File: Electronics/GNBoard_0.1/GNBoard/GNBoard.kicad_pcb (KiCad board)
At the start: 2 copper layers, 77.9 x 54.5 mm, 47 parts, among them K1 IR1, K10 IR4, K11 CNY_1, K12 CNY_2, K13 CNY_3, K14 CNY_4, K15 CNY_5, K16 CNY_6, K2 IR2, K3 SERVO_1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

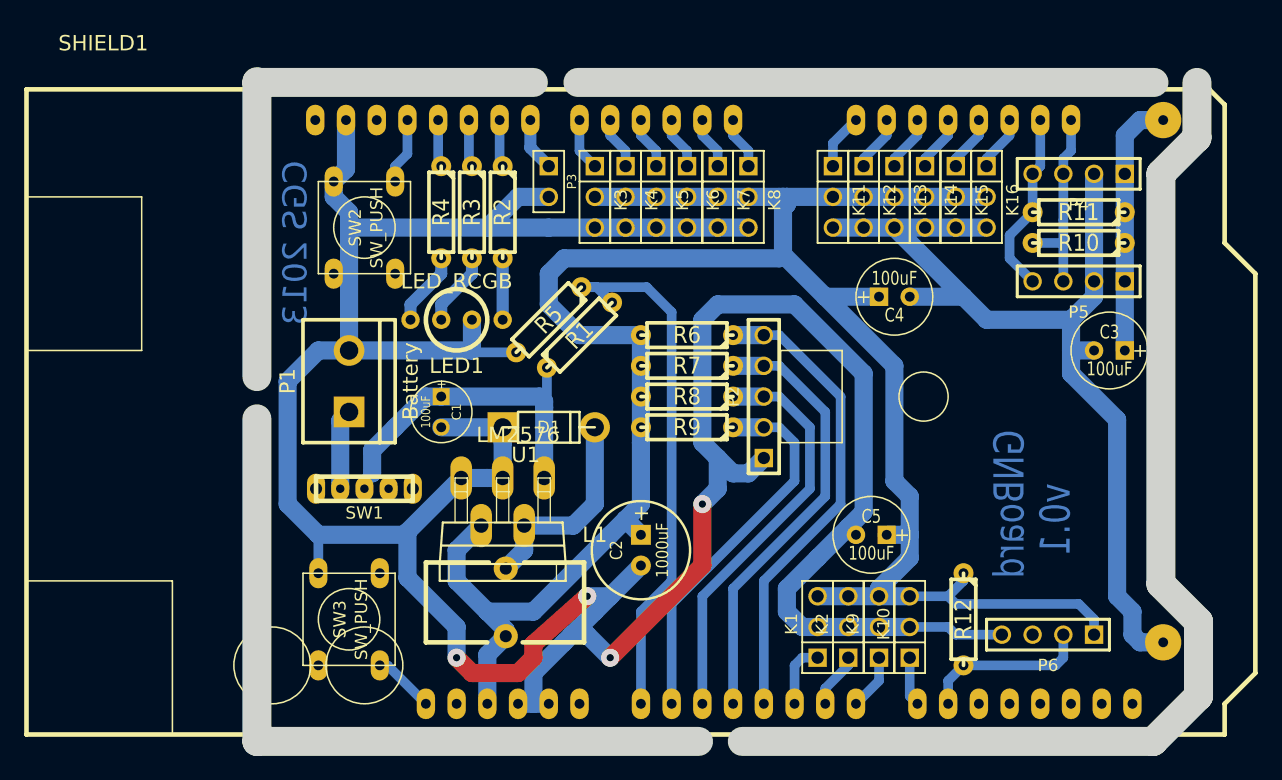
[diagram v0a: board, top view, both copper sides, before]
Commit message: Updated value of the resistors for the battery voltage monitor
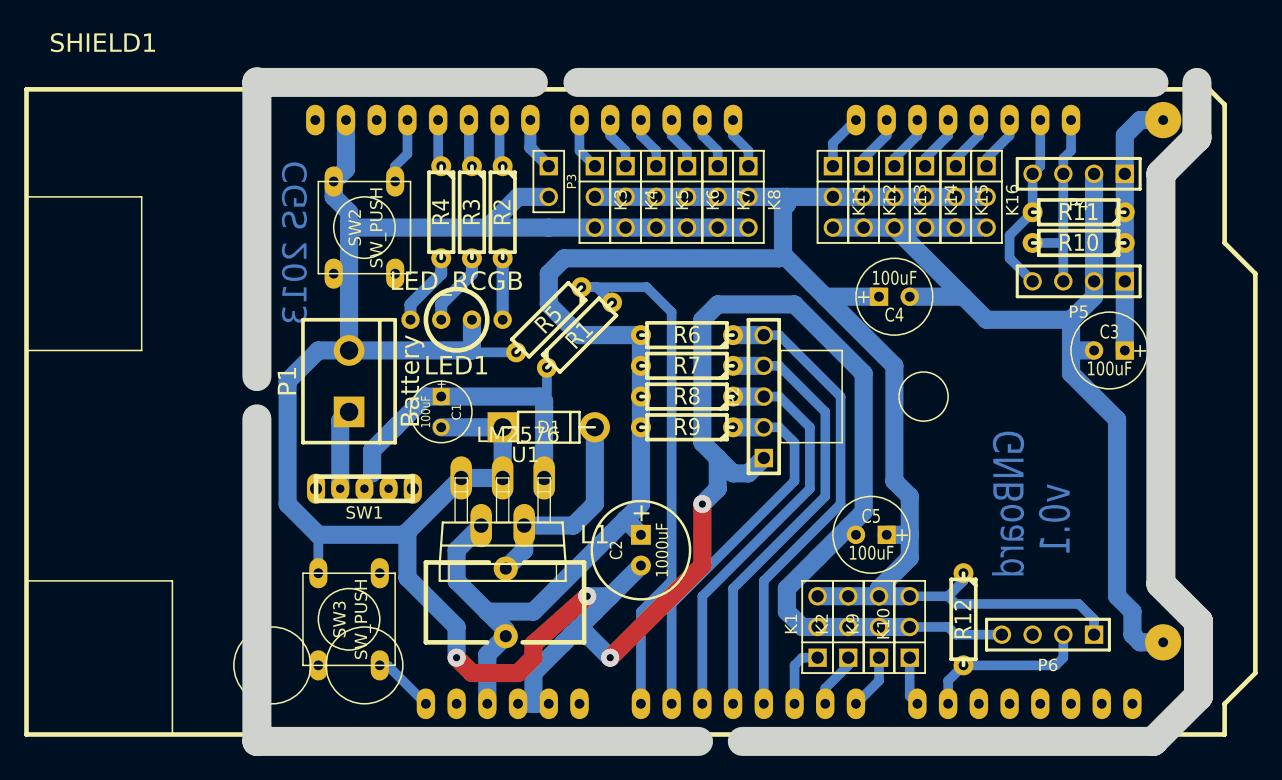
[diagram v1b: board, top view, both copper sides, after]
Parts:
- R1: value 6k8 -> 22k
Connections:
- P6 pad 3: N-0000082 -> (no net)
- SHIELD1 pad 13: N-0000067 -> (no net)
- SHIELD1 pad 3V3: N-0000040 -> (no net)
- SHIELD1 pad AD10: N-0000041 -> (no net)
- SHIELD1 pad AD11: N-0000039 -> (no net)
- SHIELD1 pad AD12: N-0000042 -> (no net)
- SHIELD1 pad AD13: N-0000043 -> (no net)
- SHIELD1 pad AD14: N-0000044 -> (no net)
- SHIELD1 pad AD15: N-0000045 -> (no net)
- SHIELD1 pad AREF: N-0000037 -> (no net)
- SHIELD1 pad V_IN: N-0000038 -> (no net)
- SW1 pad 3: N-0000046 -> (no net)
